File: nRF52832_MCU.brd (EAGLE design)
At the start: 35.2 x 23.3 mm, 31 parts, among them J100 DEBUG_CONNECTOR, P1 WIREPADSMD1,27-254, P2 WIREPADSMD1,27-254, P3 WIREPADSMD1,27-254, P4 WIREPADSMD1,27-254, U1 NRF52832, X1 32MHz, X2 32.768kHz

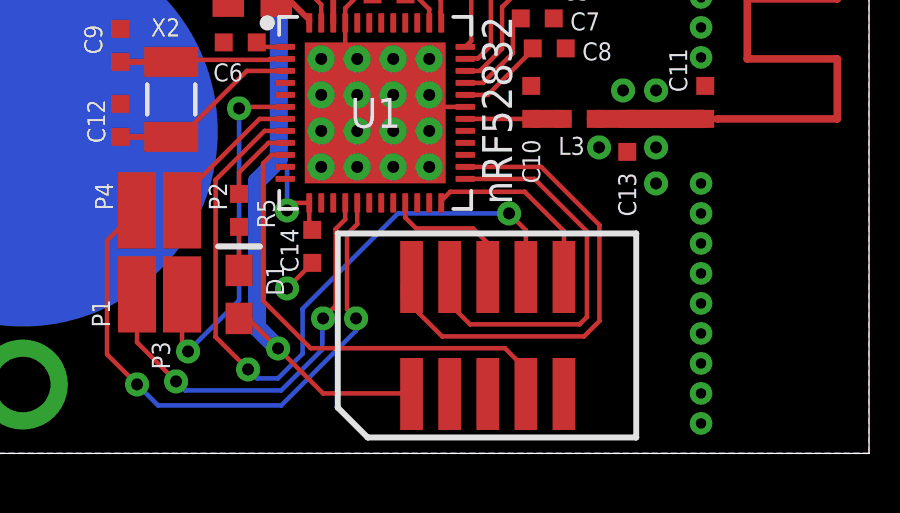
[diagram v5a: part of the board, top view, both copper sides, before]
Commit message: Add space for further devices
Accelerometer, pressure,..
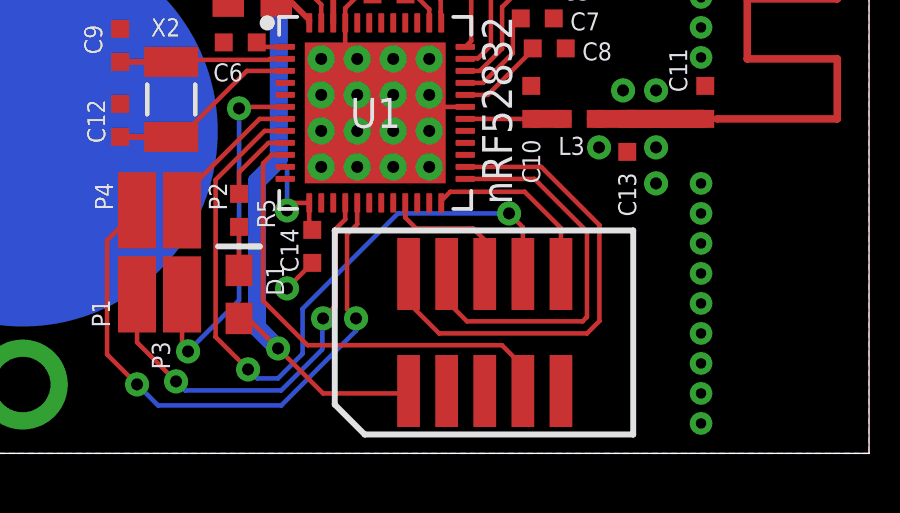
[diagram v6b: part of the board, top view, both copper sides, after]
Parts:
- moved J100 0.14 mm to (22.4, 4.03)
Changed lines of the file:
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@@
 <attribute name="NAME" x="12.24" y="14.5" size="0.6" layer="25" rot="R180"/>
 </element>
-<element name="J100" library="Nordic_misc" package="HDRV127P5X2-10_N" value="DEBUG_CONNECTOR" x="22.49" y="3.93" smashed="yes">
-<attribute name="BGA" x="22.49" y="3.93" size="1.778" layer="27" display="off"/>
+<element name="J100" library="Nordic_misc" package="HDRV127P5X2-10_N" value="DEBUG_CONNECTOR" x="22.39" y="4.03" smashed="yes">
+<attribute name="BGA" x="22.39" y="4.03" size="1.778" layer="27" display="off"/>
 </element>
 <element name="C13" library="Nordic_misc" package="RESC0402_N" value="N.C." x="27.14" y="10.6" smashed="yes" rot="R270">
@@
 <wire x1="17.74" y1="14.35" x2="17.74" y2="14.84" width="0.1524" layer="1"/>
 <wire x1="17.74" y1="14.84" x2="18.2" y2="15.3" width="0.1524" layer="1"/>
-<wire x1="27.14" y1="10.05" x2="29.74" y2="12.25" width="0" layer="19" extent="1-1"/>
-<wire x1="22.49" y1="1.98" x2="25.03" y2="1.98" width="0" layer="19" extent="1-1"/>
 </signal>
 <signal name="DEC1">
@@
 <via x="14.5" y="2.8" extent="1-16" drill="0.4"/>
 <via x="23.2" y="8" extent="1-16" drill="0.4"/>
-<wire x1="23.76" y1="7.44" x2="23.2" y2="8" width="0.1524" layer="1"/>
-<wire x1="23.76" y1="7.44" x2="23.76" y2="5.88" width="0.1524" layer="1"/>
+<wire x1="23.66" y1="7.54" x2="23.2" y2="8" width="0.1524" layer="1"/>
+<wire x1="23.66" y1="7.54" x2="23.66" y2="5.98" width="0.1524" layer="1"/>
 <wire x1="15.74" y1="10.75" x2="15.05" y2="10.75" width="0.1524" layer="1"/>
 <wire x1="15.05" y1="10.75" x2="13.4188" y2="9.1188" width="0.1524" layer="1"/>
@@
 <signal name="P0.08_RX">
 <contactref element="J100" pad="7"/>
-<wire x1="23.76" y1="1.98" x2="23.76" y2="2.80989375" width="0.1524" layer="1"/>
-<wire x1="23.76" y1="2.80989375" x2="23.06369375" y2="3.5062" width="0.1524" layer="1"/>
-<wire x1="16.58390625" y1="3.5062" x2="15" y2="5.09010625" width="0.1524" layer="1"/>
+<wire x1="23.66" y1="2.08" x2="23.66" y2="2.90989375" width="0.1524" layer="1"/>
+<wire x1="23.66" y1="2.90989375" x2="22.96369375" y2="3.6062" width="0.1524" layer="1"/>
+<wire x1="16.48390625" y1="3.6062" x2="15" y2="5.09010625" width="0.1524" layer="1"/>
 <wire x1="15" y1="5.09010625" x2="15" y2="9.66510625" width="0.1524" layer="1"/>
-<wire x1="23.06369375" y1="3.5062" x2="16.58390625" y2="3.5062" width="0.1524" layer="1"/>
+<wire x1="22.96369375" y1="3.6062" x2="16.48390625" y2="3.6062" width="0.1524" layer="1"/>
 <contactref element="U1" pad="10"/>
 <wire x1="15.28489375" y1="9.95" x2="15.74" y2="9.95" width="0.1524" layer="1"/>
@@
 <wire x1="19.74" y1="8.35" x2="19.74" y2="7.86" width="0.1524" layer="1"/>
 <wire x1="20.1" y1="7.5" x2="22" y2="7.5" width="0.1524" layer="1"/>
-<wire x1="22" y1="7.5" x2="22.49" y2="7.01" width="0.1524" layer="1"/>
-<wire x1="22.49" y1="7.01" x2="22.49" y2="5.88" width="0.1524" layer="1"/>
+<wire x1="22" y1="7.5" x2="22.39" y2="7.11" width="0.1524" layer="1"/>
+<wire x1="22.39" y1="7.11" x2="22.39" y2="5.98" width="0.1524" layer="1"/>
 <wire x1="19.74" y1="7.86" x2="20.1" y2="7.5" width="0.1524" layer="1"/>
 <contactref element="U1" pad="21"/>
@@
 <signal name="P0.21/RESET">
 <contactref element="J100" pad="10"/>
-<wire x1="25.03" y1="7.41" x2="23.72" y2="8.72" width="0.1524" layer="1"/>
+<wire x1="24.93" y1="7.51" x2="23.72" y2="8.72" width="0.1524" layer="1"/>
 <wire x1="21.24" y1="8.72" x2="20.94" y2="8.42" width="0.1524" layer="1"/>
 <wire x1="20.94" y1="8.35" x2="20.94" y2="8.42" width="0.1524" layer="1"/>
 <wire x1="23.72" y1="8.72" x2="21.24" y2="8.72" width="0.1524" layer="1"/>
-<wire x1="25.03" y1="7.41" x2="25.03" y2="5.88" width="0.1524" layer="1"/>
+<wire x1="24.93" y1="7.51" x2="24.93" y2="5.98" width="0.1524" layer="1"/>
 <contactref element="U1" pad="24"/>
 </signal>
@@
 <wire x1="25.79686875" y1="7.39926875" x2="24.0461375" y2="9.15" width="0.1524" layer="1"/>
 <wire x1="25.79686875" y1="7.39926875" x2="25.79686875" y2="4.546975" width="0.1524" layer="1"/>
-<wire x1="25.79686875" y1="4.546975" x2="25.55229375" y2="4.3024" width="0.1524" layer="1"/>
-<wire x1="21.8976" y1="4.3024" x2="21.2" y2="5" width="0.1524" layer="1"/>
-<wire x1="21.2" y1="5" x2="21.2" y2="5.86" width="0.1524" layer="1"/>
-<wire x1="21.2" y1="5.86" x2="21.22" y2="5.88" width="0.1524" layer="1"/>
-<wire x1="25.55229375" y1="4.3024" x2="21.8976" y2="4.3024" width="0.1524" layer="1"/>
+<wire x1="25.79686875" y1="4.546975" x2="25.65229375" y2="4.4024" width="0.1524" layer="1"/>
+<wire x1="21.7976" y1="4.4024" x2="21.2" y2="5" width="0.1524" layer="1"/>
+<wire x1="21.2" y1="5" x2="21.2" y2="5.9" width="0.1524" layer="1"/>
+<wire x1="21.2" y1="5.9" x2="21.12" y2="5.98" width="0.1524" layer="1"/>
+<wire x1="25.65229375" y1="4.4024" x2="21.7976" y2="4.4024" width="0.1524" layer="1"/>
 <contactref element="U1" pad="25"/>
 </signal>
@@
 <contactref element="J100" pad="2"/>
 <wire x1="24.2738" y1="9.55" x2="21.74" y2="9.55" width="0.1524" layer="1"/>
-<wire x1="19.95" y1="5.88" x2="19.67" y2="5.6" width="0.1524" layer="1"/>
-<wire x1="19.67" y1="5.6" x2="19.67" y2="5.2" width="0.1524" layer="1"/>
+<wire x1="19.85" y1="5.98" x2="19.67" y2="5.8" width="0.1524" layer="1"/>
+<wire x1="19.67" y1="5.8" x2="19.67" y2="5.2" width="0.1524" layer="1"/>
 <wire x1="26.2119" y1="7.6119" x2="24.2738" y2="9.55" width="0.1524" layer="1"/>
-<wire x1="25.7" y1="3.9" x2="26.2119" y2="4.4119" width="0.1524" layer="1"/>
+<wire x1="25.8" y1="4" x2="26.2119" y2="4.4119" width="0.1524" layer="1"/>
 <wire x1="26.2119" y1="4.4119" x2="26.2119" y2="7.6119" width="0.1524" layer="1"/>
-<wire x1="25.7" y1="3.9" x2="20.97" y2="3.9" width="0.1524" layer="1"/>
-<wire x1="20.97" y1="3.9" x2="19.67" y2="5.2" width="0.1524" layer="1"/>
+<wire x1="25.8" y1="4" x2="20.87" y2="4" width="0.1524" layer="1"/>
+<wire x1="20.87" y1="4" x2="19.67" y2="5.2" width="0.1524" layer="1"/>
 <contactref element="U1" pad="26"/>
 </signal>
@@
 <wire x1="14.5" y1="4.5" x2="14.2" y2="4.5" width="0.1524" layer="1"/>
 <contactref element="BATT1" pad="2"/>
-<wire x1="19.95" y1="1.98" x2="19.95" y2="2" width="0.1524" layer="1"/>
-<wire x1="19.95" y1="2" x2="17" y2="2" width="0.1524" layer="1"/>
+<wire x1="19.85" y1="2.08" x2="19.85" y2="2" width="0.1524" layer="1"/>
+<wire x1="19.85" y1="2" x2="17" y2="2" width="0.1524" layer="1"/>
 <wire x1="17" y1="2" x2="15.5" y2="3.5" width="0.1524" layer="1"/>
 <via x="14.5" y="16.2" extent="1-16" drill="0.4"/>

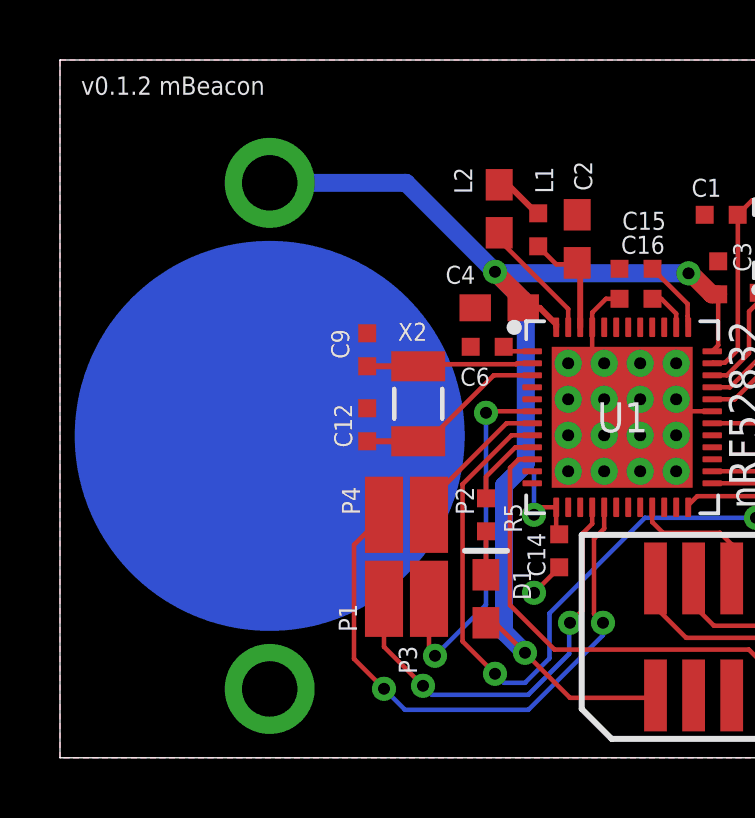
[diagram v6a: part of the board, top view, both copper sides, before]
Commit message: Make sure rastnest is around battery
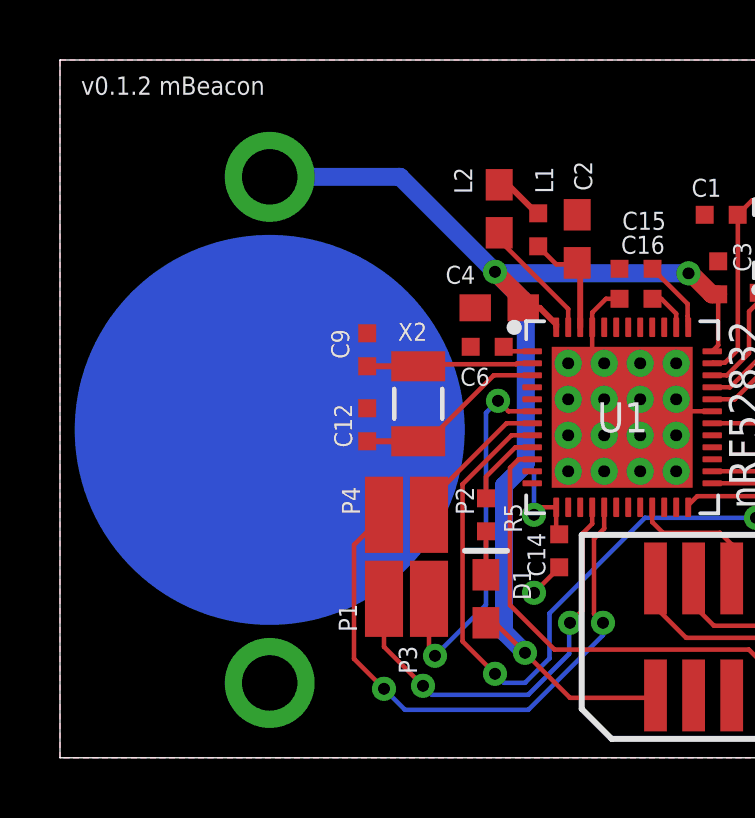
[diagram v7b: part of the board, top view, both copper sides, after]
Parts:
- moved BATT1 0.20 mm to (6.99, 10.9)
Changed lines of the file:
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@@
 <attribute name="NAME" x="9.14" y="11.8" size="0.6" layer="25" rot="R270"/>
 </element>
-<element name="BATT1" library="Nordic_misc" package="CR1632_HOLDER_TH" value="CR1632" x="6.99" y="10.73" smashed="yes" rot="MR270"/>
+<element name="BATT1" library="Nordic_misc" package="CR1632_HOLDER_TH" value="CR1632" x="6.99" y="10.93" smashed="yes" rot="MR270"/>
 <element name="D1" library="Nordic_misc" package="DIOC0603_N" value="LED" x="14.2" y="5.3" smashed="yes" rot="R270">
 <attribute name="NAME" x="15.1" y="6.3" size="0.6" layer="25" rot="R270"/>
@@
 <signal name="P0.04">
 <contactref element="P3" pad="1"/>
-<wire x1="14.2" y1="11.5" x2="14.25" y2="11.55" width="0.1524" layer="1"/>
-<wire x1="15.74" y1="11.55" x2="14.25" y2="11.55" width="0.1524" layer="1"/>
-<via x="14.2" y="11.5" extent="1-16" drill="0.4"/>
+<wire x1="14.6" y1="11.9" x2="14.95" y2="11.55" width="0.1524" layer="1"/>
+<wire x1="15.74" y1="11.55" x2="14.95" y2="11.55" width="0.1524" layer="1"/>
+<via x="14.6" y="11.9" extent="1-16" drill="0.4"/>
+<wire x1="14.6" y1="11.9" x2="14.2" y2="11.5" width="0.1524" layer="16"/>
 <wire x1="14.2" y1="11.5" x2="14.2" y2="5.1" width="0.1524" layer="16"/>
 <wire x1="14.2" y1="5.1" x2="12.5" y2="3.4" width="0.1524" layer="16"/>
@@
 <wire x1="17" y1="2" x2="15.5" y2="3.5" width="0.1524" layer="1"/>
 <via x="14.5" y="16.2" extent="1-16" drill="0.4"/>
-<wire x1="6.99" y1="19.165" x2="11.535" y2="19.165" width="0.6" layer="16"/>
+<wire x1="6.99" y1="19.365" x2="11.335" y2="19.365" width="0.6" layer="16"/>
 <wire x1="21.94" y1="15.45" x2="21.94" y2="13.75" width="0.1524" layer="1"/>
 <wire x1="21.74" y1="13.55" x2="21.94" y2="13.75" width="0.1524" layer="1"/>
@@
 <wire x1="14.5" y1="16.2" x2="15.44" y2="15.26" width="0.6" layer="1"/>
 <wire x1="15.525" y1="15.175" x2="14.5" y2="16.2" width="0.6" layer="16"/>
-<wire x1="14.5" y1="16.2" x2="11.535" y2="19.165" width="0.6" layer="16"/>
+<wire x1="14.5" y1="16.2" x2="11.335" y2="19.365" width="0.6" layer="16"/>
 <via x="15.5" y="3.5" extent="1-16" drill="0.4"/>
 <wire x1="15.5" y1="3.5" x2="14.8" y2="4.2" width="0.6" layer="16"/>
